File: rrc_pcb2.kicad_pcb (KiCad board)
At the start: 2 copper layers, 124.5 x 64.4 mm, 15 parts, among them J1 Conn_01x02_Male-Connector, J2 Conn_01x03_Male-Connector, J3 Conn_01x02_Male-Connector, J4 Conn_01x02_Female, U1 iridium9602, U2 Teensy4.1, U3 BN220-GPS, U4 ICM-20948, U5 MS5611, U6 logo

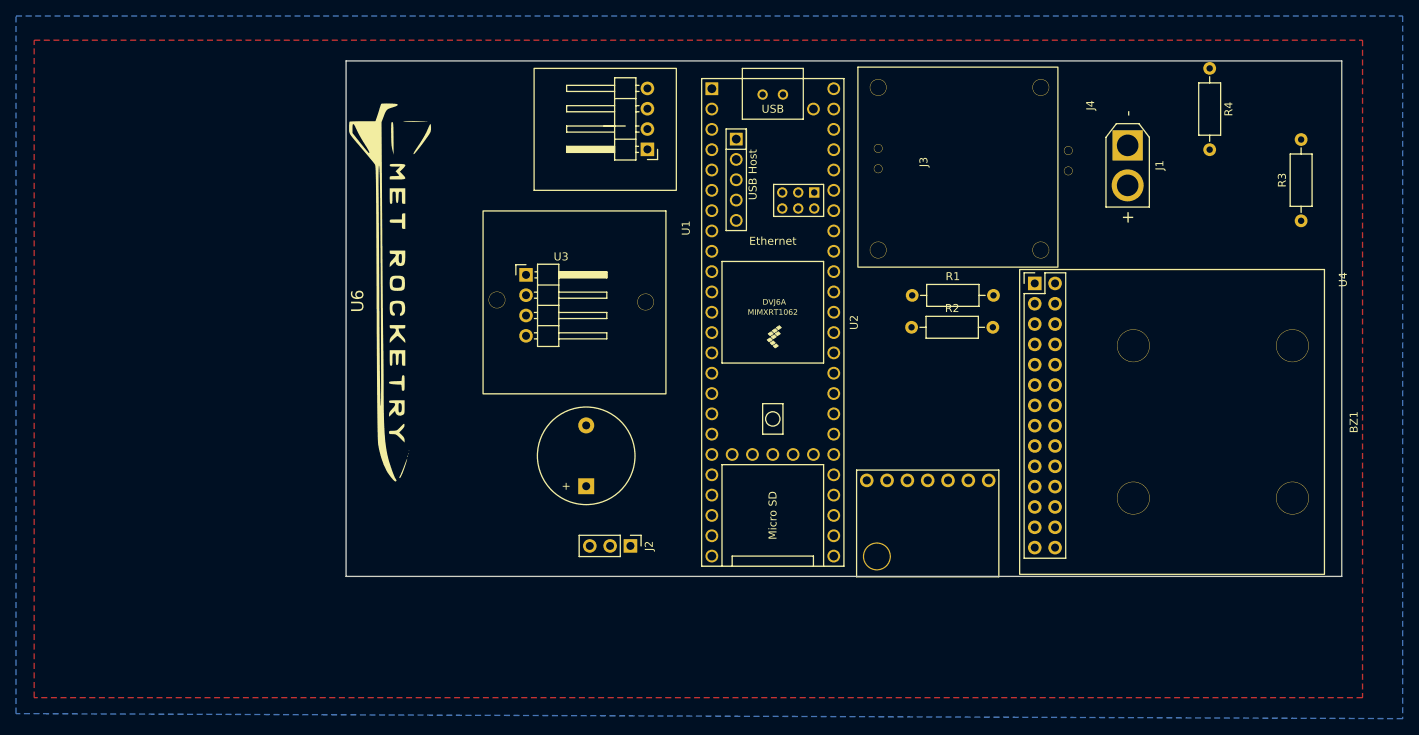
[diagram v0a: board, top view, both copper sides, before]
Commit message: tweaked srad main board
tweaked iridium footprints and volt reg footprints and added a back board just in case iridium doenst pan out; uses rfd900p instead.
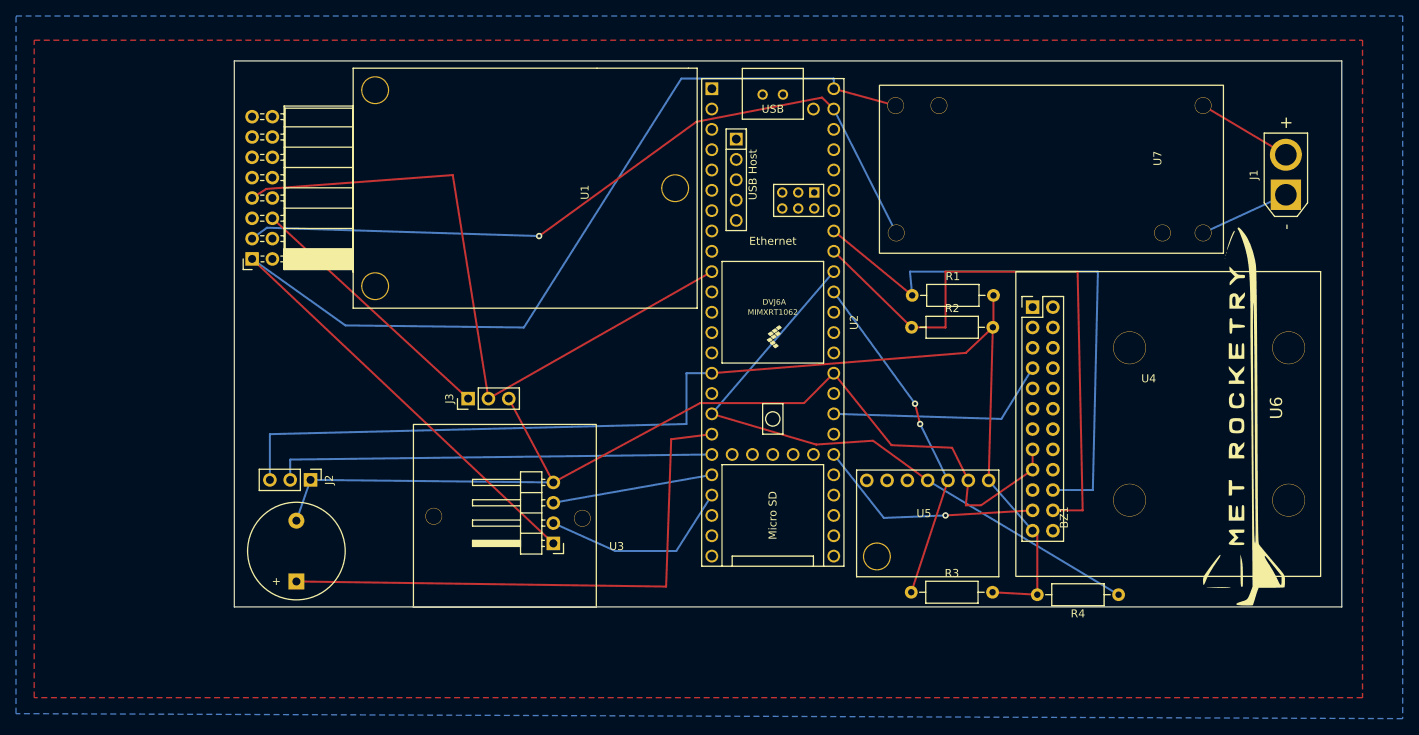
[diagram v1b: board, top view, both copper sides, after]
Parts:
- removed J4: Conn_01x02_Female, Connector_PinSocket_2.54mm:PinSocket_2x01_P2.54mm_Horizontal
- added U7: Conn_01x02_Male-Connector, VoltReg:voltReg, F.Cu at (165.6, 44.7)
- J3: value Conn_01x02_Male-Connector -> digital logic connection; footprint Connector_PinSocket_2.54mm:PinSocket_1x02_P2.54mm_Horizontal -> Connector_PinHeader_2.54mm:PinHeader_1x03_P2.54mm_Vertical
- U1: value iridium9602 -> RFD900+; footprint Connector_PinHeader_2.54mm:PinHeader_1x04_P2.54mm_Horizontal -> rfd900+:RFD900+
- U3: footprint Connector_PinHeader_2.54mm:PinHeader_1x04_P2.54mm_Horizontal -> bn220_gps:BN220
- U4: footprint Connector_PinHeader_2.54mm:PinHeader_2x14_P2.54mm_Vertical -> icm20948:icm20948
- moved U6 108.6 mm to (168.0, 68.1), turned to 90 degrees
- moved R3 67.3 mm to (126.5, 87.1), turned to 0 degrees
- moved R4 66.8 mm to (152.4, 87.4), turned to 180 degrees
- moved J3 64.0 mm to (71.1, 62.9), turned to 90 degrees
- moved U3 41.3 mm to (64.3, 66.1), turned to 0 degrees
- moved J2 40.8 mm to (51.4, 73.0)
- moved BZ1 38.1 mm to (49.7, 85.7)
- moved U1 27.3 mm to (56.8, 21.6), turned to -90 degrees
- moved U4 26.1 mm to (156.2, 60.9), turned to 0 degrees
- moved J1 20.7 mm to (173.4, 37.4), turned to 90 degrees
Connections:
- net RX1 renamed RX7
- net SCL2 renamed SCL
- net SDA2 renamed SDA
- net TX1 renamed TX7
- J1 pad 1: 7.2V -> Net-(J1-Pad1)
- J1 pad 2: GND -> Net-(J1-Pad2)
- J3 pad 1: VCC -> RX2
- J3 pad 2: GND -> TX2
- U1 pad 2: TX2 -> unconnected-(U1-Pad2)
- U1 pad 3: RX2 -> GND
- U1 pad 4: GND -> unconnected-(U1-Pad4)
- U2 pad 38: SDA1 -> SCL1
- U2 pad 39: SCL1 -> SDA1
- U4 pad 9: (no net) -> unconnected-(U4-Pad9)
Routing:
- net VCC: track 0.00 -> 153.6 mm
- net T_VCC: track 0.00 -> 149.2 mm
- net T_GND: track 0.00 -> 125.8 mm
- net GND: track 0.00 -> 96.0 mm, vias 0 -> 1
- net TX2: track 0.00 -> 85.9 mm
- net SDA1: track 0.00 -> 80.4 mm
- net SDA: track 0.00 -> 74.9 mm
- net SCL: track 0.00 -> 71.5 mm
- net Net-(BZ1-Pad1): track 0.00 -> 69.8 mm
- net Net-(J2-Pad2): track 0.00 -> 55.2 mm
- net SCL1: track 0.00 -> 42.5 mm, vias 0 -> 2
- net RX2: track 0.00 -> 33.3 mm
- net FSYNC: track 0.00 -> 28.7 mm, vias 0 -> 1
- net INT1: track 0.00 -> 28.4 mm
- net TX7: track 0.00 -> 24.4 mm
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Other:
- board size 124.5 x 64.4 mm -> 138.4 x 68.2 mm

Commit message: Edit of PCB
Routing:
- net SDA1: track 80.4 -> 70.8 mm, vias 0 -> 1

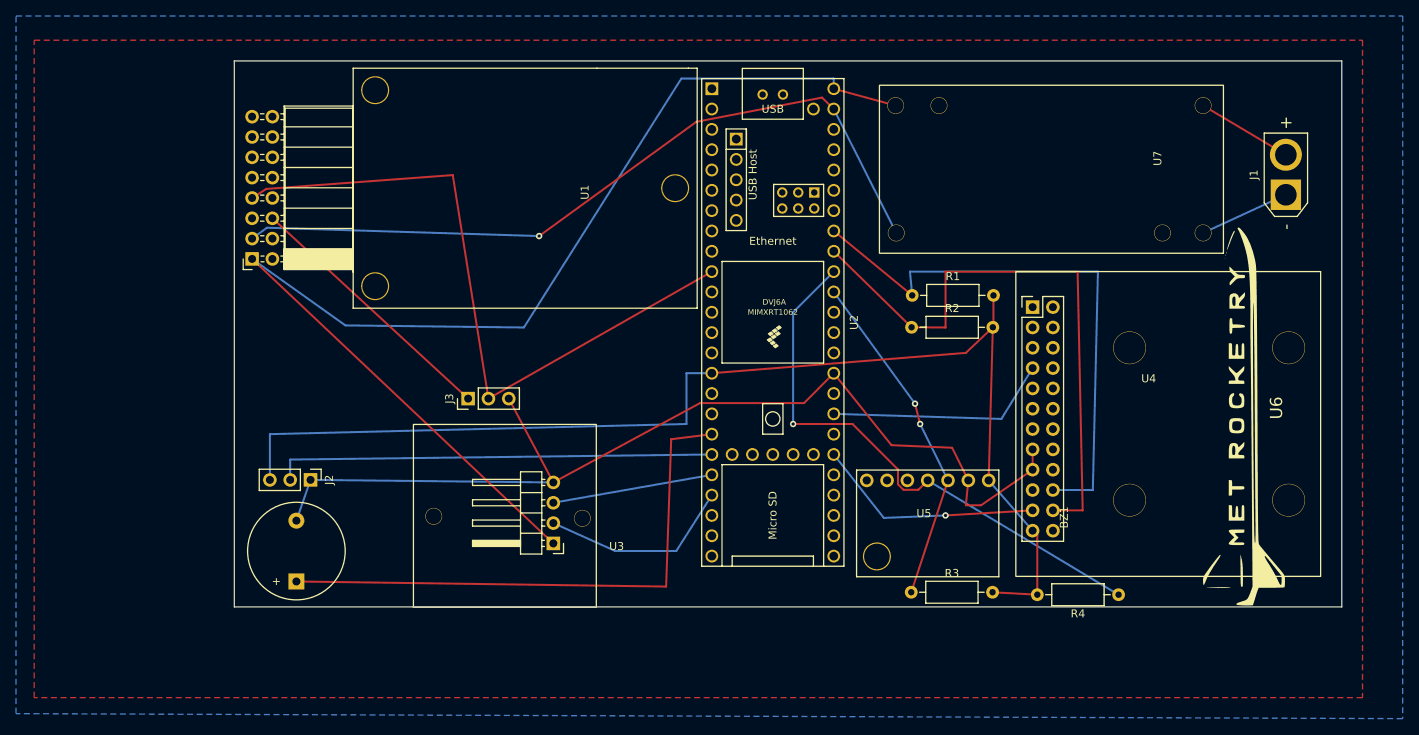
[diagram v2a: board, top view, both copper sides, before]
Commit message: pcb update with new volt reg
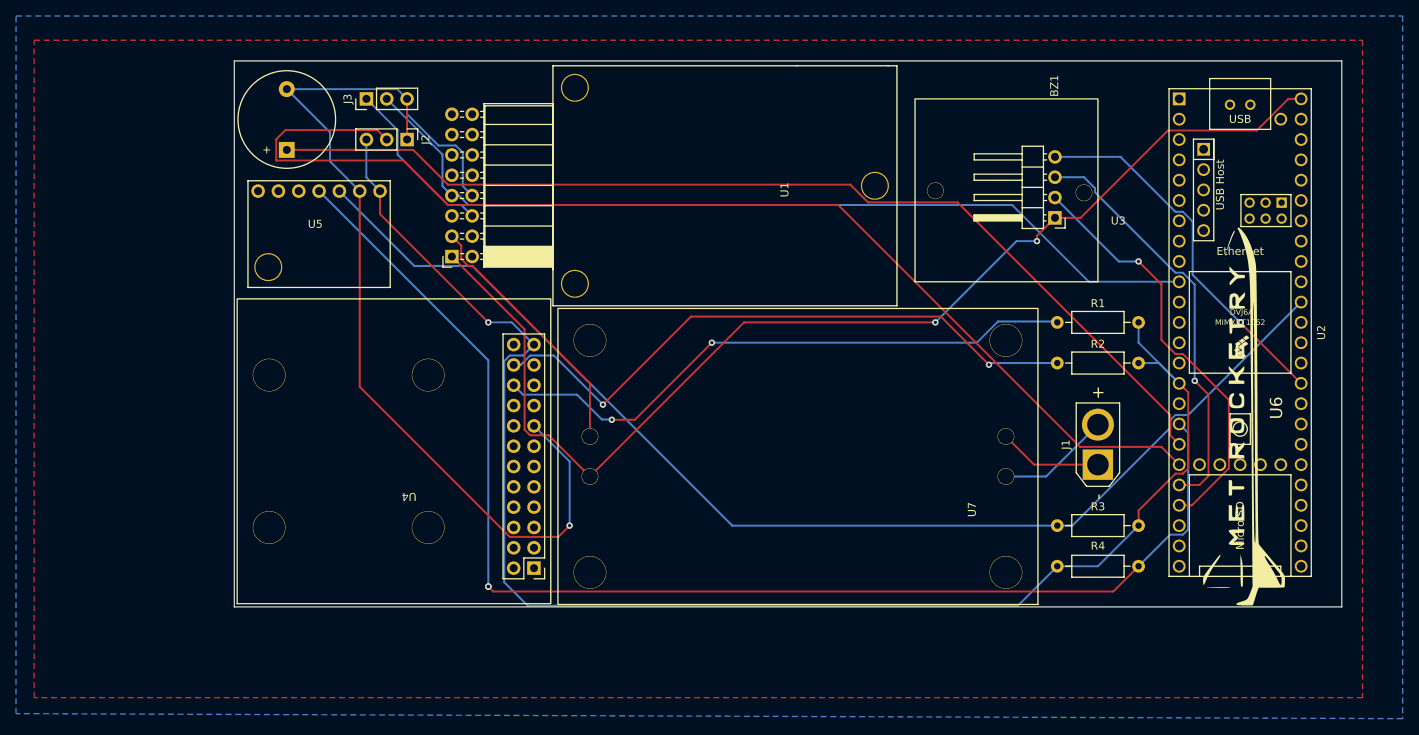
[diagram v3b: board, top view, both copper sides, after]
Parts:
- moved U4 93.5 mm to (63.8, 74.6), turned to 180 degrees
- moved U5 84.2 mm to (52.5, 33.1)
- moved U3 74.8 mm to (127.0, 25.4)
- moved U2 58.4 mm to (167.6, 54.6)
- moved BZ1 54.0 mm to (48.5, 31.8)
- moved U7 49.7 mm to (142.4, 88.6)
- moved J2 44.2 mm to (63.5, 30.5)
- moved J1 41.1 mm to (149.9, 71.1)
- moved J3 39.6 mm to (58.4, 25.4)
- moved U1 25.0 mm to (81.7, 21.3)
- moved R3 20.1 mm to (144.8, 78.7)
- moved R2 18.8 mm to (144.8, 58.4)
- moved R1 18.4 mm to (144.8, 53.3)
- moved R4 4.35 mm to (154.9, 83.8)
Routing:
- net SCL1: track 42.5 -> 149.7 mm, vias 2 -> 0
- net SDA1: track 70.8 -> 162.8 mm, vias 1 -> 2
- net Net-(J2-Pad2): track 55.2 -> 146.1 mm
- net GND: track 96.0 -> 32.8 mm, vias 1 -> 0
- net Net-(BZ1-Pad1): track 69.8 -> 128.3 mm
- net T_GND: track 125.8 -> 173.6 mm, vias 0 -> 3
- net T_VCC: track 149.2 -> 190.1 mm, vias 0 -> 1
- net RX7: track 20.1 -> 52.3 mm, vias 0 -> 1
- net FSYNC: track 28.7 -> 0.00 mm, vias 1 -> 0
- net TX7: track 24.4 -> 53.0 mm, vias 0 -> 1
- net INT1: track 28.4 -> 0.00 mm
- net TX2: track 85.9 -> 110.8 mm
- net RX2: track 33.3 -> 21.1 mm
- net VCC: track 153.6 -> 144.8 mm, vias 0 -> 2
- net SCL: track 71.5 -> 74.9 mm, vias 0 -> 2
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
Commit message: new pcb designs w/ new volt reg
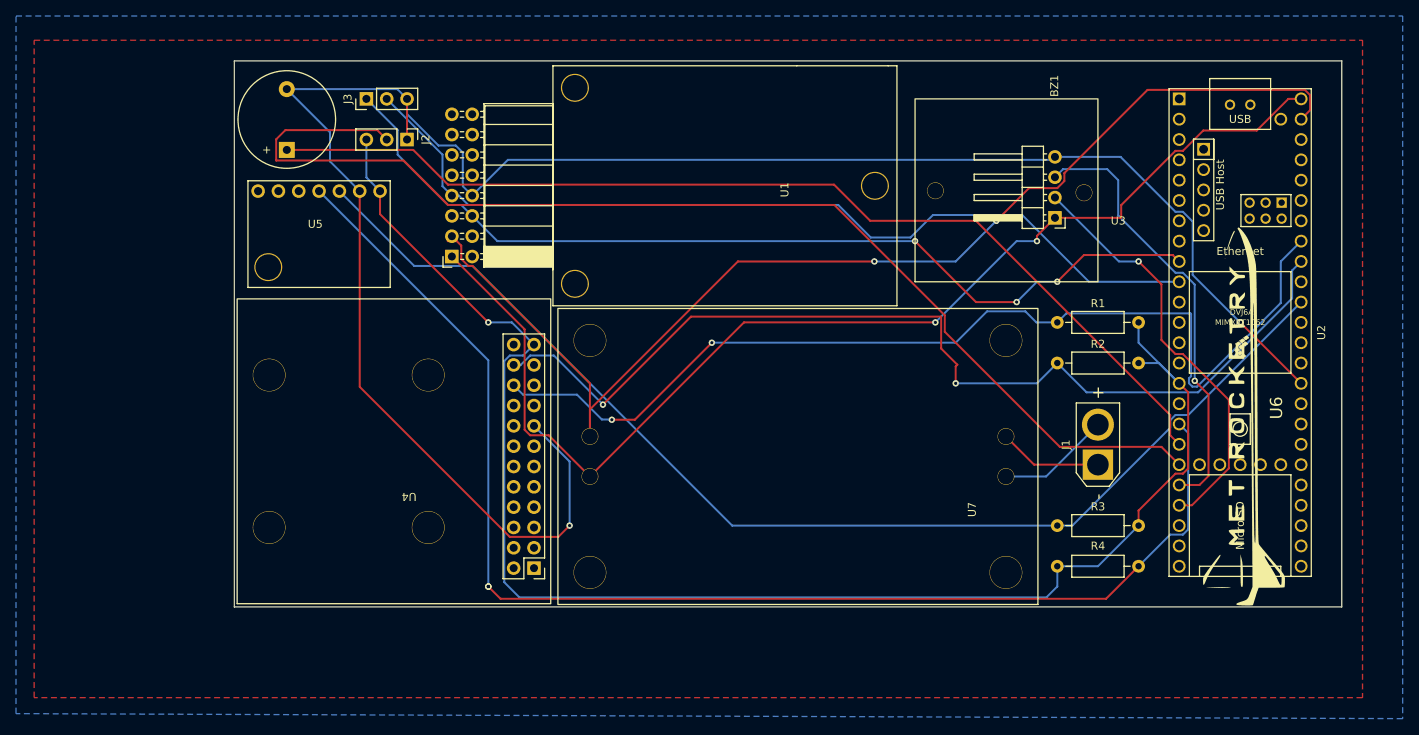
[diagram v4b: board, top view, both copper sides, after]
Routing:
- net GND: track 32.8 -> 147.0 mm, vias 0 -> 2
- net RX2: track 21.1 -> 116.7 mm, vias 0 -> 3
- net T_GND: track 173.6 -> 248.5 mm
- net SCL: track 74.9 -> 126.7 mm
- net SDA: track 78.2 -> 125.1 mm
- net RX7: track 52.3 -> 55.4 mm
- net TX2: track 110.8 -> 113.2 mm
- net Net-(J2-Pad2): track 146.1 -> 147.3 mm
- net VCC: track 144.8 -> 145.8 mm
- net SDA1: track 162.8 -> 163.5 mm
- net T_VCC: track 190.1 -> 190.7 mm

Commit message: R1&R2 removed
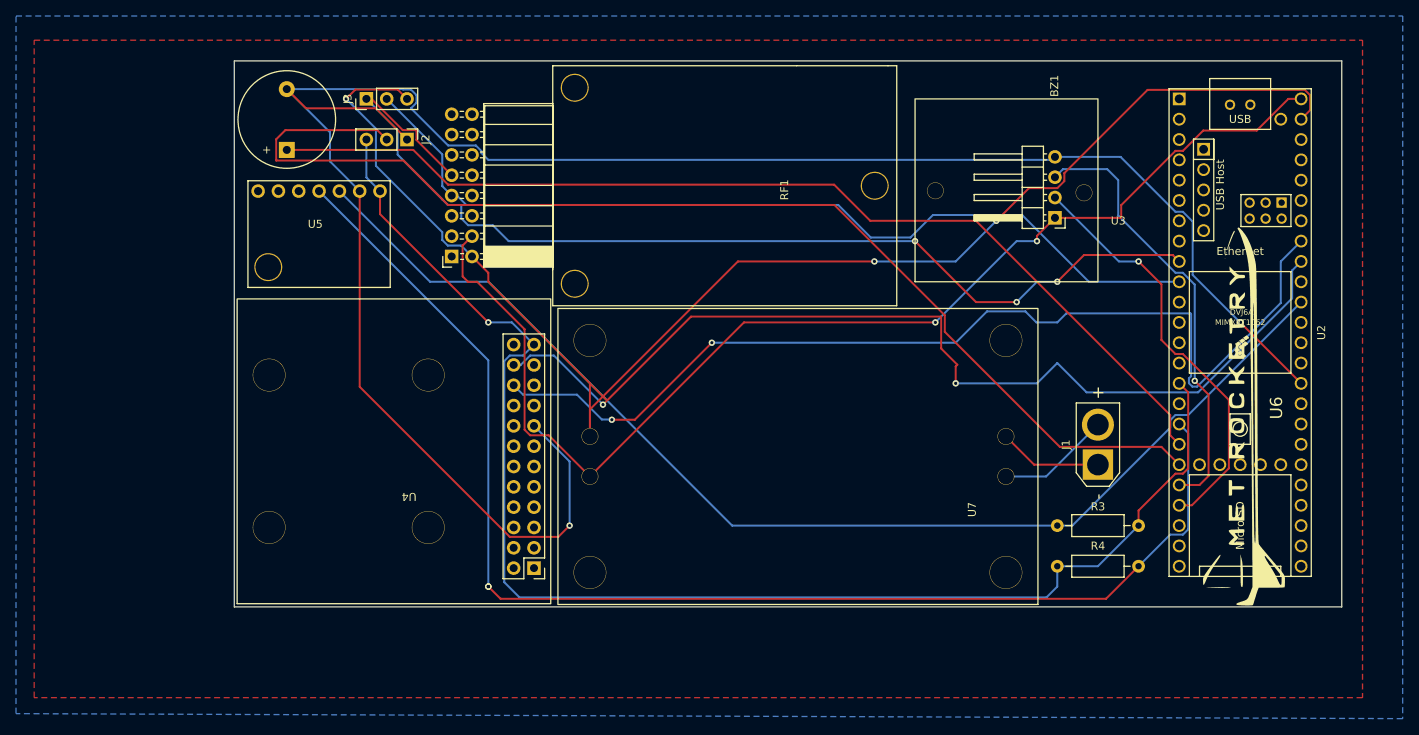
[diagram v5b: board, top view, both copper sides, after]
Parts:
- removed R1, R2: R-Device, Resistor_THT:R_Axial_DIN0207_L6.3mm_D2.5mm_P10.16mm_Horizontal
- removed U1: RFD900+, rfd900+:RFD900+
- added RF1: RFD900+-RF_Module, rfd900+:RFD900+, F.Cu at (81.7, 21.3)
- U7: value Conn_01x02_Male-Connector -> voltReg
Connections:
- J3 pad 3: T_GND -> GND
- U4 pad 24: unconnected-(U4-Pad24) -> VCC
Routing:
- net GND: track 147.0 -> 181.5 mm, vias 2 -> 3
- net RX2: track 116.7 -> 133.0 mm
- net T_VCC: track 190.7 -> 174.9 mm
- net T_GND: track 248.5 -> 255.9 mm
- net VCC: track 145.8 -> 148.9 mm

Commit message: UPDATED IMU and fixed some mounting holes
replaced imu with mpu6050 and fixed batt header footprint and organized stuff
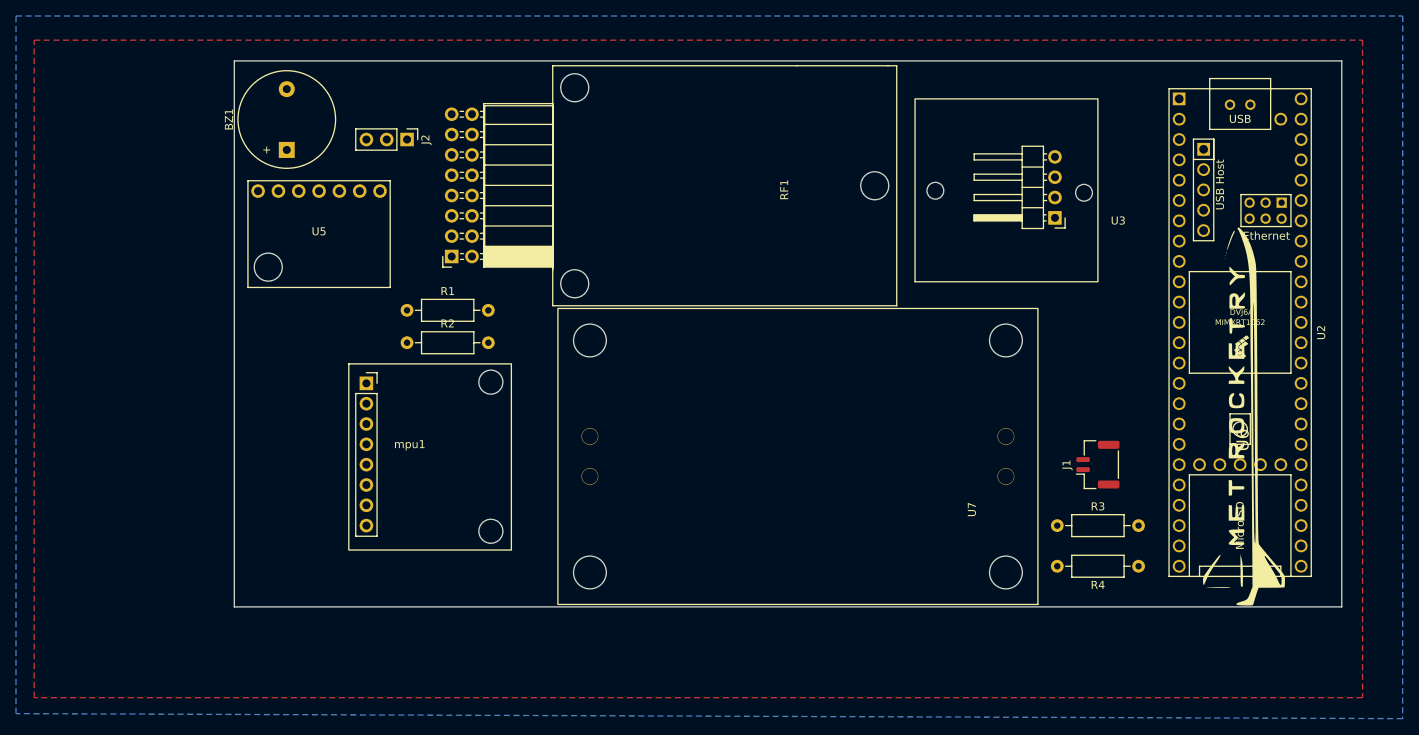
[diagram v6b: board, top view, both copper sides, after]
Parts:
- removed J3: digital logic connection, Connector_PinHeader_2.54mm:PinHeader_1x03_P2.54mm_Vertical
- removed U4: ICM-20948, icm20948:icm20948
- added R1: R-Device, Resistor_THT:R_Axial_DIN0207_L6.3mm_D2.5mm_P10.16mm_Horizontal, F.Cu at (63.5, 51.8)
- added R2: R-Device, Resistor_THT:R_Axial_DIN0207_L6.3mm_D2.5mm_P10.16mm_Horizontal, F.Cu at (63.5, 55.9)
- added mpu1: ~, MPU6050:MPU6050, F.Cu at (63.8, 69.1)
- J1: value Conn_01x02_Male-Connector -> battery_header; footprint Connector_AMASS:AMASS_XT30U-F_1x02_P5.0mm_Vertical -> Connector_JST:JST_GH_SM02B-GHS-TB_1x02-1MP_P1.25mm_Horizontal
- J2: value Conn_01x03_Male-Connector -> buzzer_toggle_pin
- U7: value voltReg -> Conn_01x02_Male-Connector
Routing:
- net T_GND: track 255.9 -> 0.00 mm, vias 3 -> 0
- net GND: track 181.5 -> 0.00 mm, vias 3 -> 0
- net T_VCC: track 174.9 -> 0.00 mm, vias 1 -> 0
- net SDA1: track 163.5 -> 0.00 mm, vias 2 -> 0
- net SCL1: track 149.7 -> 0.00 mm
- net VCC: track 148.9 -> 0.00 mm, vias 2 -> 0
- net Net-(J2-Pin_2): track 147.3 -> 0.00 mm
- net RX2: track 133.0 -> 0.00 mm, vias 3 -> 0
- net Net-(BZ1--): track 128.3 -> 0.00 mm
- net SCL: track 126.7 -> 0.00 mm, vias 2 -> 0
- net SDA: track 125.1 -> 0.00 mm, vias 2 -> 0
- net TX2: track 113.2 -> 0.00 mm
- net RX7: track 55.4 -> 0.00 mm, vias 1 -> 0
- net TX7: track 53.0 -> 0.00 mm, vias 1 -> 0
- net Net-(J1-Pin_2): track 14.2 -> 0.00 mm
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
